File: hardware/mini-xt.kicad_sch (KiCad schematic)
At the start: 0 parts

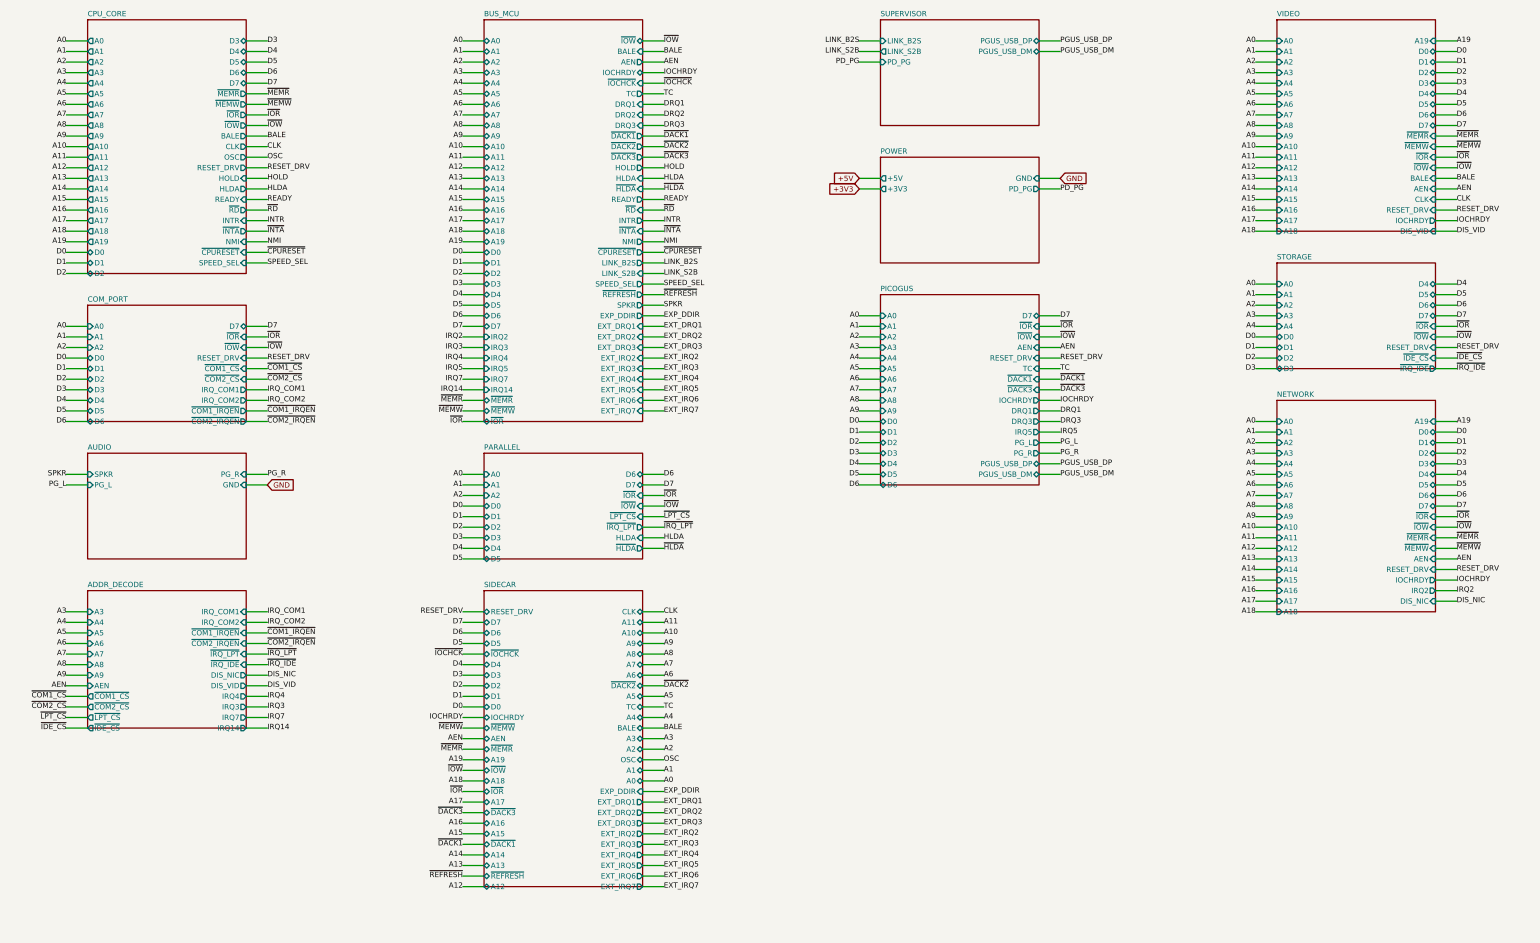
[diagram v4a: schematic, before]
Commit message: Remove the on-board RTL8019AS NIC (tag full-board-with-nic preserves it)
Network sheet, symbols, and NIC-only parts.py bindings deleted; addr_decode
JP6->JP5 (DIS_VID); IRQ2 retired as an internal net like IRQ6/IRQ8 (still
reachable as EXT_IRQ2 from the expansion port). ERC stays 0/0.

Co-Authored-By: Claude Fable 5 <noreply@anthropic.com>
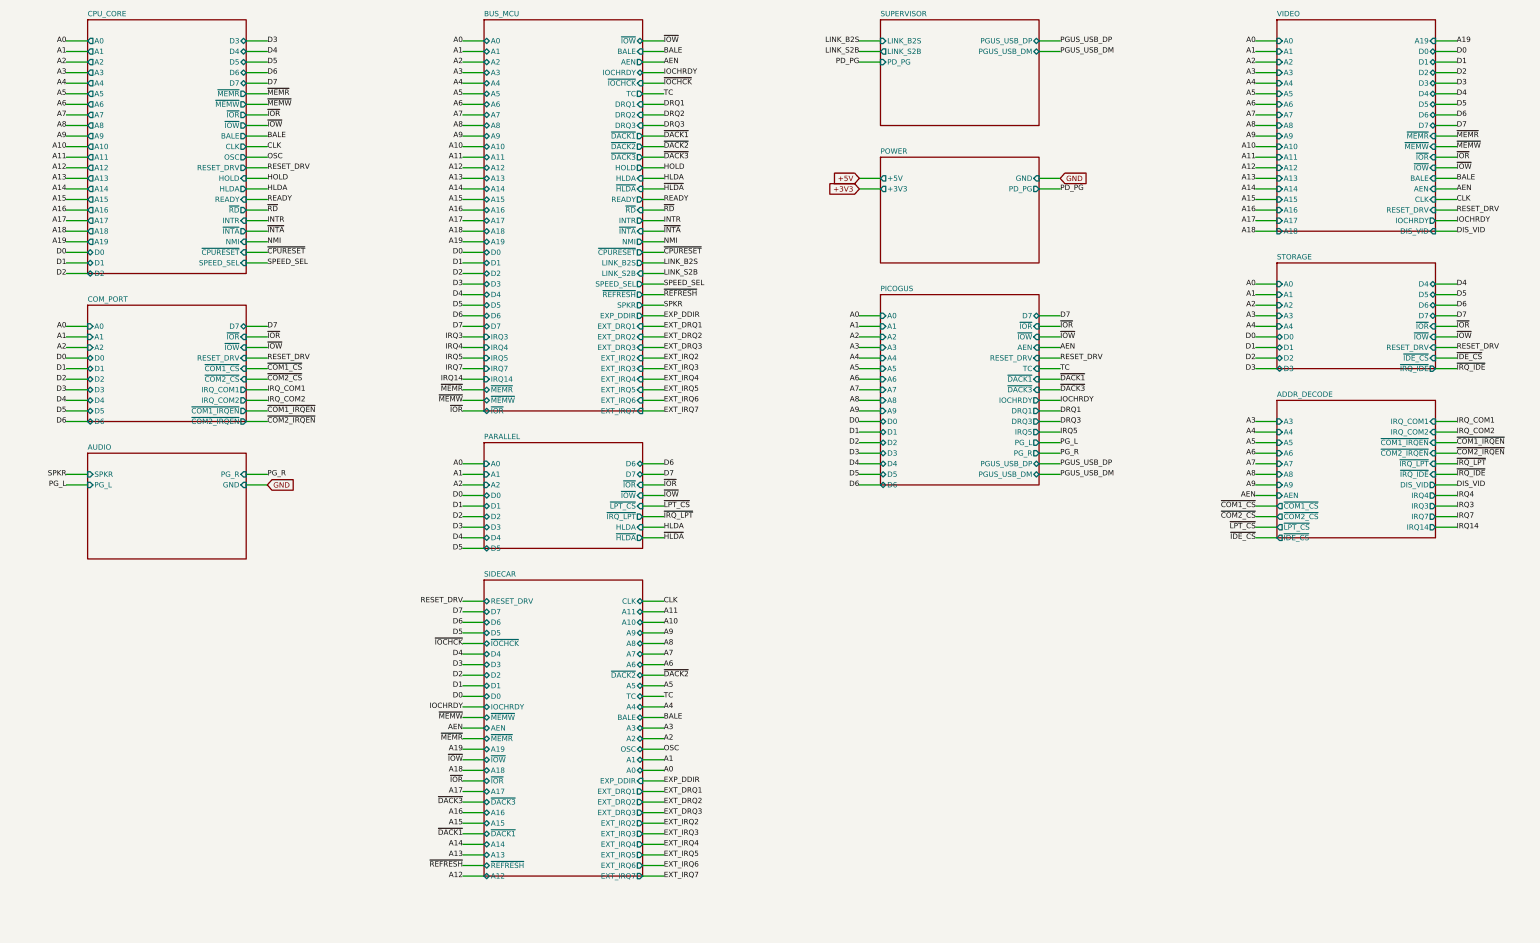
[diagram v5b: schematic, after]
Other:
- removed sheet NETWORK
- sheet ADDR_DECODE ports: added none; removed DIS_NIC
- sheet BUS_MCU ports: added none; removed IRQ2

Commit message: Expansion port: 50-pin header, port DMA channel, dev cards deleted
Two waves of the 2026-07-14/15 expansion-port rework (the first was
uncommitted): the IRQ-scan collapse to one '165 + '32 OR rank with
ISA-card DMA removed outright, then the port redesign that brings one
DMA channel back:

- isa_conn: 60-pin (2x30, PicoGUS-standard layout) -> 50-pin (2x25,
  project-private pinout; 50-way IDC is far easier to source). OSC and
  ~REFRESH dropped to fit (no on-board consumer / no DRAM refresh; the
  planned ISA backplane board re-creates both for period cards).
- Port DMA: EXT_DRQ rides the sidecar inbound '244 + U12 '165 spare D6
  lane (zero GPIO); ~EXT_DACK = GPIO47 (freed by ~REFRESH) out through
  the strobe '244. Separate nets from the internal PicoGUS pair, so a
  port card never sees the on-board acknowledge.
- DRQ1/~DACK1 renamed DRQ/~DACK (ch2/3 long retired); DRQ2/3 +
  ~DACK2/3 removed from the mxbus contract.
- card_video + card_isatest deleted (sheets, hardware/cards/,
  build_cards()); superseded by the backplane plan. History has them.
- Connector parts: IDE header -> shrouded 2x20 IDC box (C9138, keypin
  20 NC'd); expansion port -> 90-degree 2x25 female socket (C21262364);
  addr_decode's five disable jumpers folded into ONE fixed 2x5 block
  JP1 (C492422), positions JP1.1-JP1.5 = COM1/COM2/LPT/IDE/VID.

ERC 0/0, check_parts 0 problems; docs/notes updated throughout.

Co-Authored-By: Claude Fable 5 <noreply@anthropic.com>
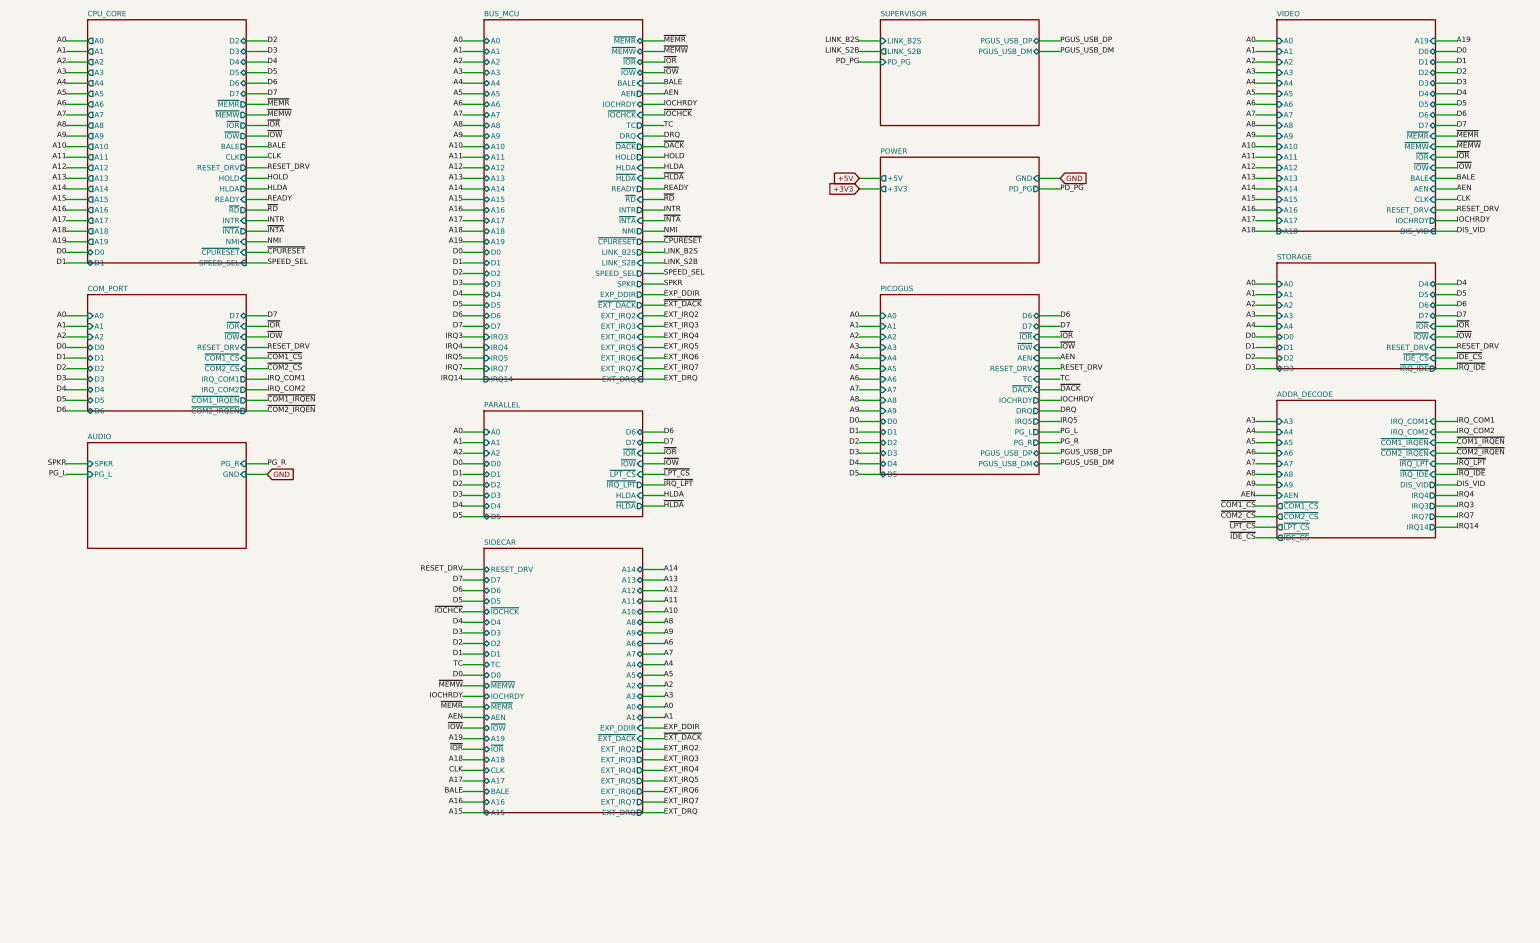
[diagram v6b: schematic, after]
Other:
- sheet BUS_MCU ports: added DRQ, EXT_DRQ, ~{DACK}, ~{EXT_DACK}; removed DRQ1, DRQ2, DRQ3, EXT_DRQ1, EXT_DRQ2, EXT_DRQ3, ~{DACK1}, ~{DACK2}, ~{DACK3}, ~{REFRESH}
- sheet CPU_CORE ports: added none; removed OSC
- sheet PICOGUS ports: added DRQ, ~{DACK}; removed DRQ1, DRQ3, ~{DACK1}, ~{DACK3}
- sheet SIDECAR ports: added EXT_DRQ, ~{EXT_DACK}; removed EXT_DRQ1, EXT_DRQ2, EXT_DRQ3, OSC, ~{DACK1}, ~{DACK2}, ~{DACK3}, ~{REFRESH}

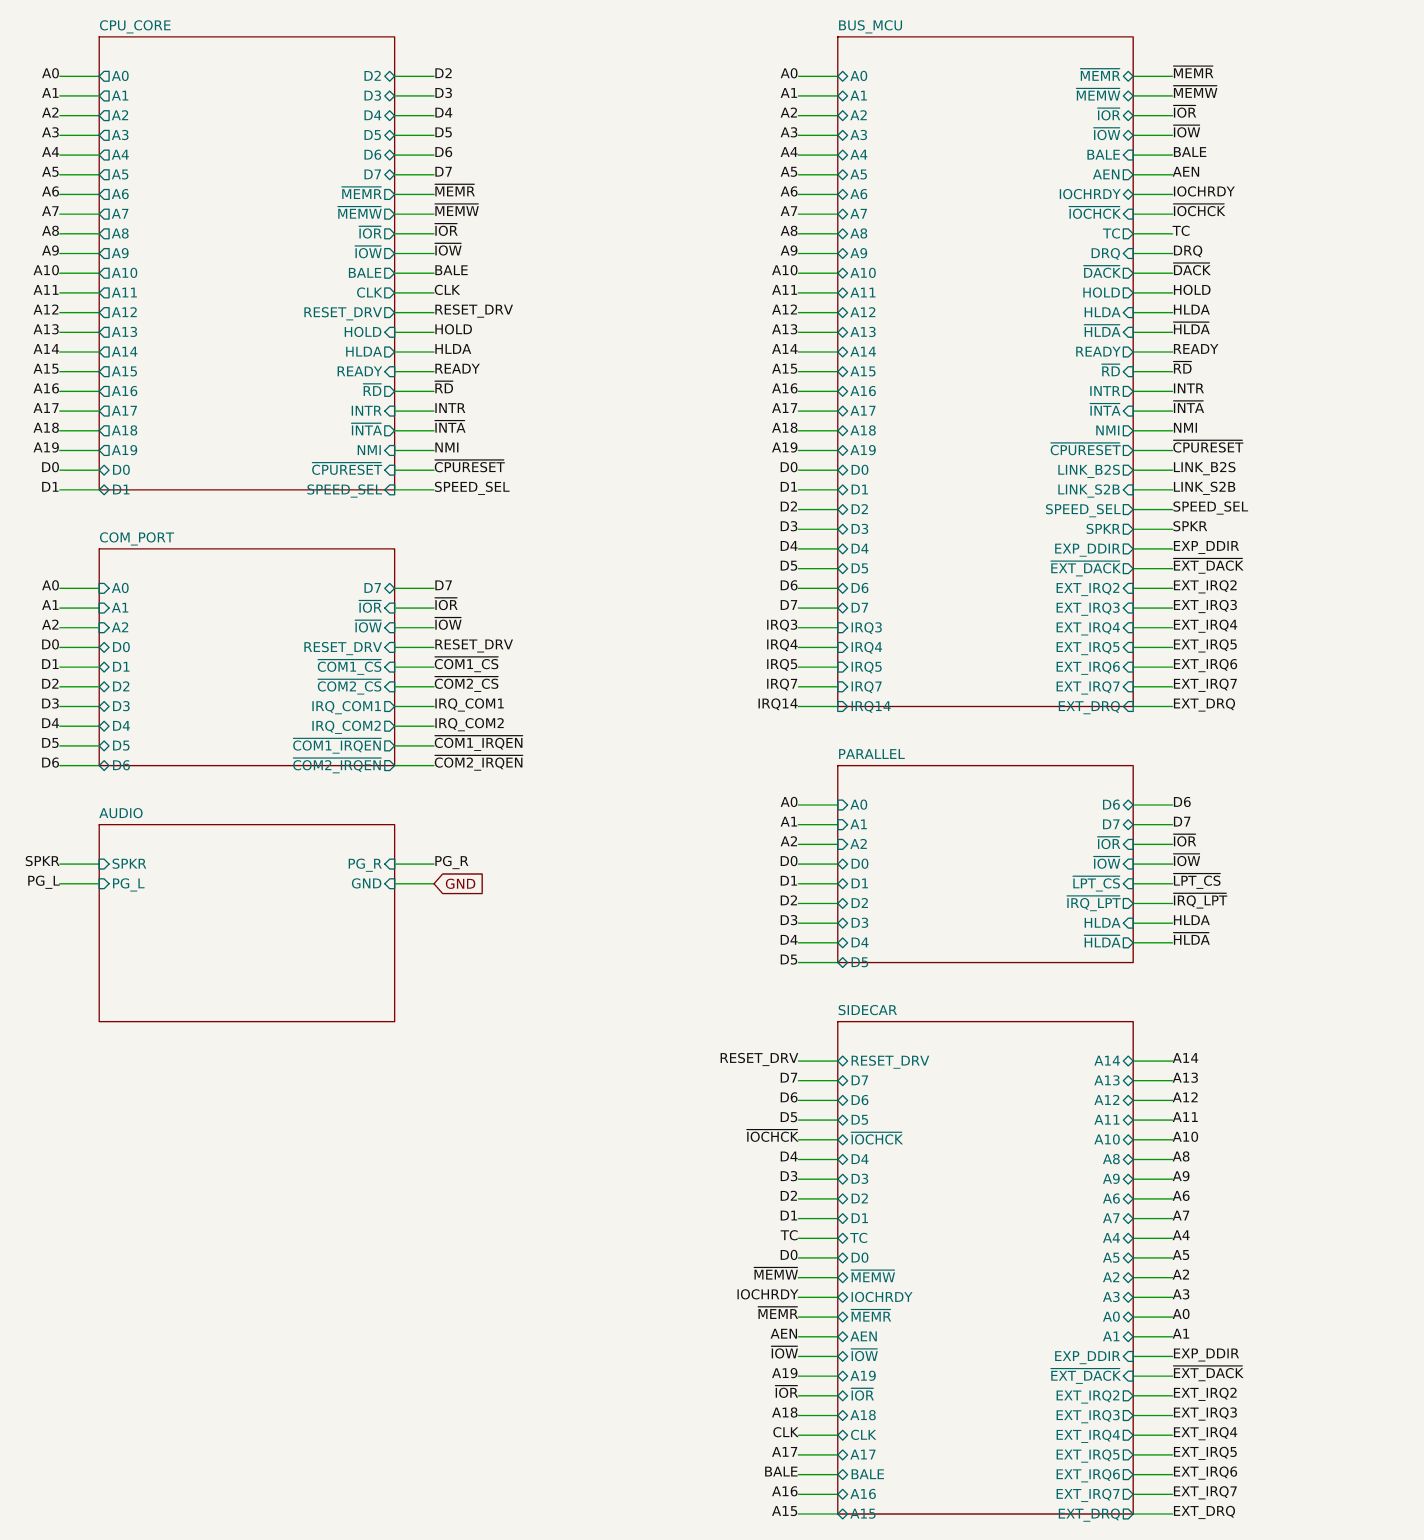
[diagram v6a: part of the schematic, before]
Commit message: Retire SPEED_SEL to a cpu_core-local jumper; docs, firmware notes, 595 prune
- SPEED_SEL leaves the private-net set: speed select is now a local strap on
  cpu_core (JP1 + 10k pulldown, open = 7.16 MHz) instead of an MCU GPIO;
  mxbus/supervisor/bus_mcu/cpu_core updated and sheets regenerated
- Add the addr_decode net-by-net I/O decode chart to docs/xt-mcu-sbc-design.md
- Add docs/bus-mcu-firmware.md and docs/video-firmware.md
- parts.py: prune the dead 74HC595 binding (last card_isatest leftover)

Co-Authored-By: Claude Fable 5 <noreply@anthropic.com>
Claude-Session: https://claude.ai/code/session_01VpbEjRYKoR12pVJpBtbaZF
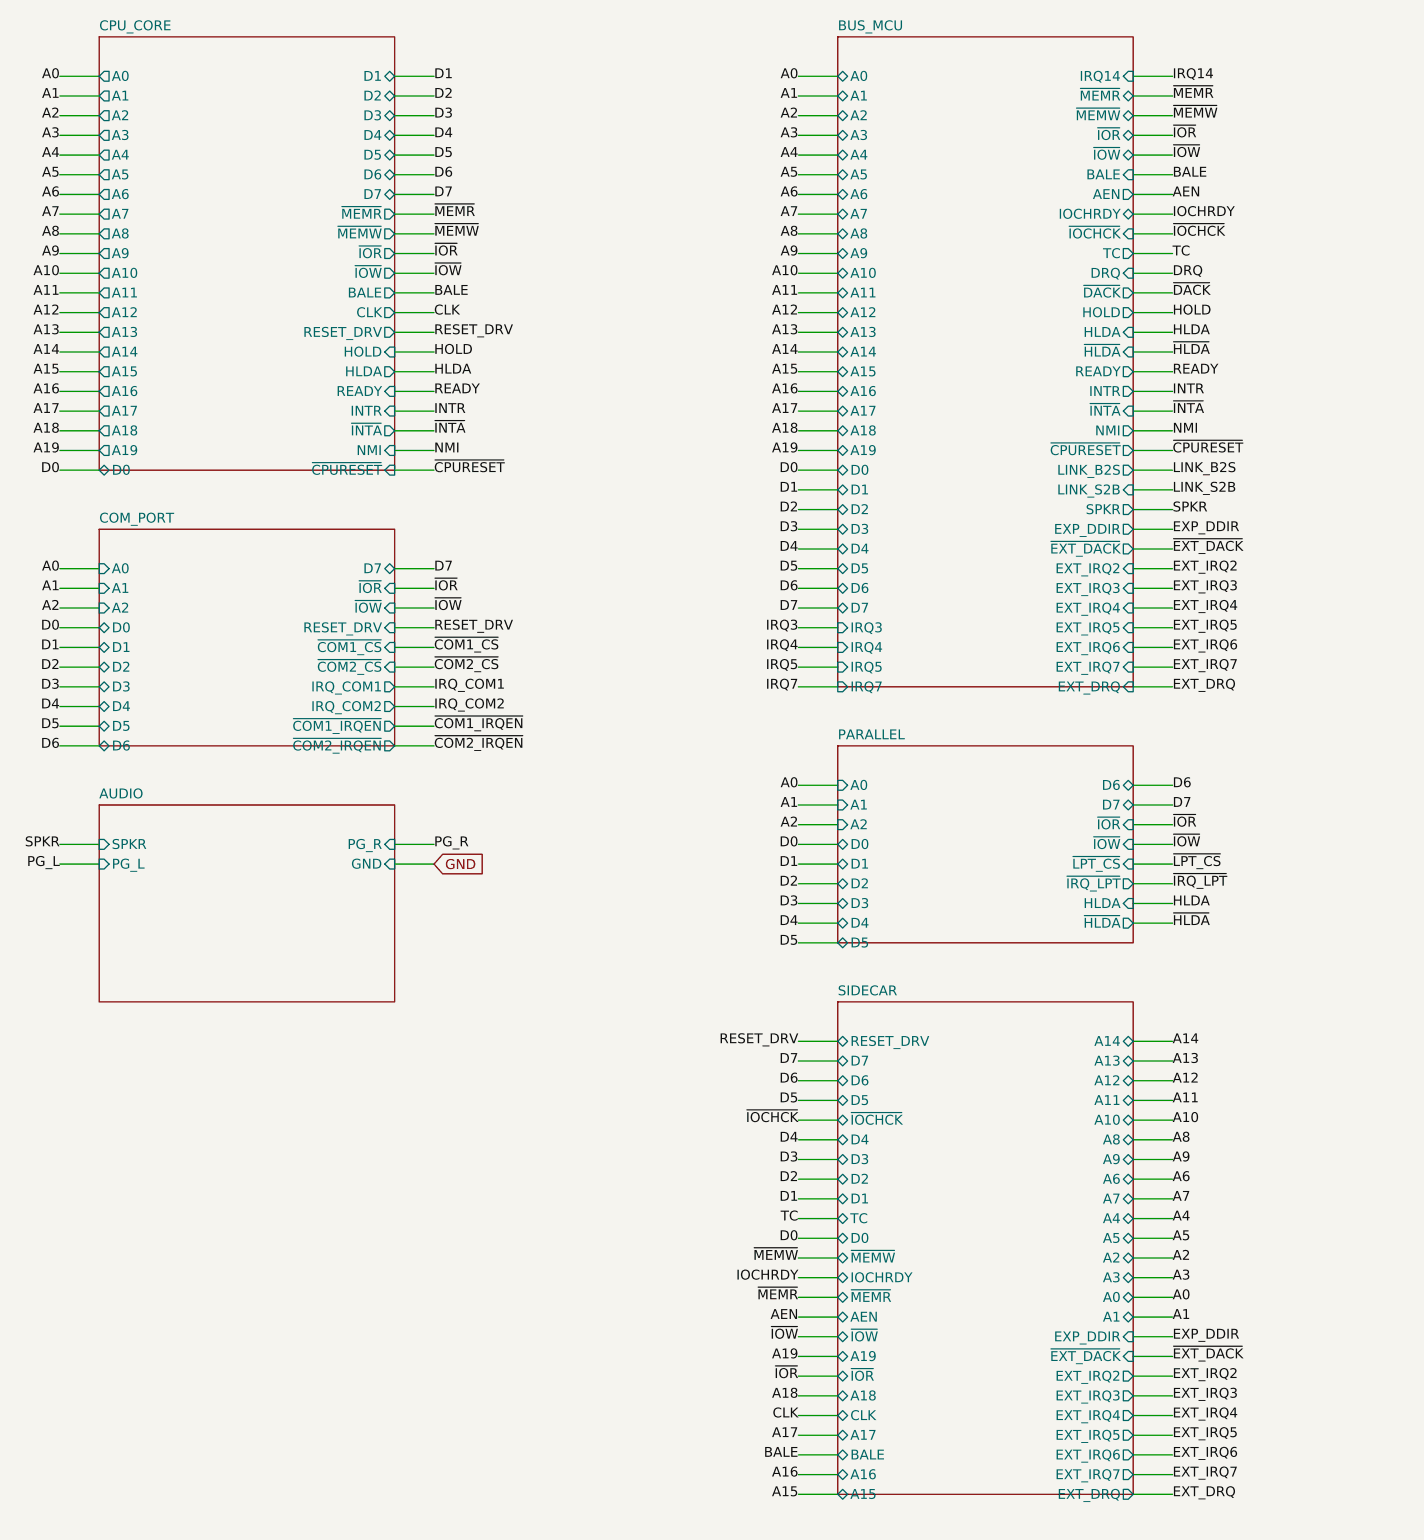
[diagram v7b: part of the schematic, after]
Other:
- sheet BUS_MCU ports: added none; removed SPEED_SEL, ~{RD}
- sheet CPU_CORE ports: added none; removed SPEED_SEL, ~{RD}
